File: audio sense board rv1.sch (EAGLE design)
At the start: 32 parts, among them IC1 A000053, IC2 TSOP38238, J1 PJRAN1X1U01X, J4 PJRAN1X1U01X, Q1 2N3904, Q2 2N3904

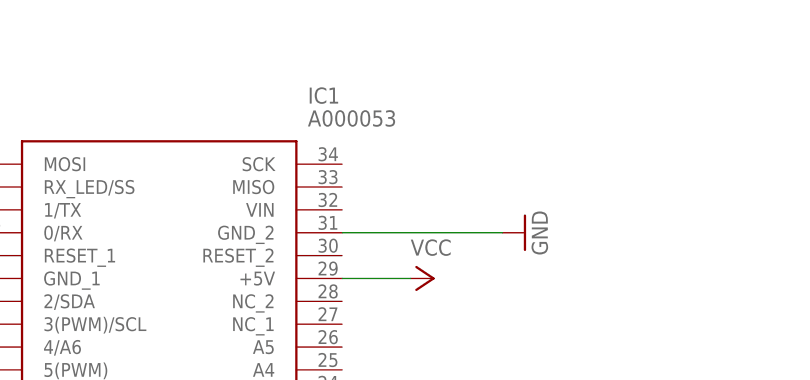
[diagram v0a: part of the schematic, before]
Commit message: add ground pour on bottom
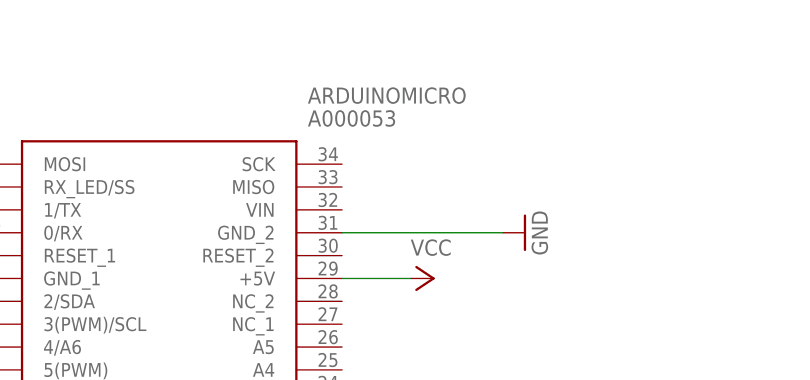
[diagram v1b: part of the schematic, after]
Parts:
- renumbered IC1 to ARDUINOMICRO
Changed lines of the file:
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@@
 <part name="R6" library="Samac Populated" deviceset="CRCW120610K0FKEAC" device="" value="10K"/>
 <part name="GND1" library="supply1" library_urn="urn:adsk.eagle:library:371" deviceset="GND" device=""/>
-<part name="IC1" library="Samac Populated" deviceset="A000053" device=""/>
+<part name="ARDUINOMICRO" library="Samac Populated" deviceset="A000053" device=""/>
 <part name="GND3" library="supply1" library_urn="urn:adsk.eagle:library:371" deviceset="GND" device=""/>
 <part name="LED2" library="SparkFun-LED" library_urn="urn:adsk.eagle:library:529" deviceset="LED" device="1206" package3d_urn="urn:adsk.eagle:package:39352/1" value="LTST-C930GKT"/>
@@
 <attribute name="VALUE" x="30.48" y="15.24" size="1.778" layer="96"/>
 </instance>
-<instance part="IC1" gate="G$1" x="-71.12" y="147.32" smashed="yes">
+<instance part="ARDUINOMICRO" gate="G$1" x="-71.12" y="147.32" smashed="yes">
 <attribute name="NAME" x="-34.29" y="154.94" size="1.778" layer="95" align="center-left"/>
 <attribute name="VALUE" x="-34.29" y="152.4" size="1.778" layer="96" align="center-left"/>
@@
 <wire x1="33.02" y1="55.88" x2="43.18" y2="55.88" width="0.1524" layer="91"/>
 <junction x="33.02" y="55.88"/>
-<pinref part="IC1" gate="G$1" pin="A1"/>
+<pinref part="ARDUINOMICRO" gate="G$1" pin="A1"/>
 <wire x1="43.18" y1="55.88" x2="43.18" y2="116.84" width="0.1524" layer="91"/>
 <wire x1="43.18" y1="116.84" x2="-30.48" y2="116.84" width="0.1524" layer="91"/>
@@
 <segment>
 <pinref part="GND3" gate="1" pin="GND"/>
-<pinref part="IC1" gate="G$1" pin="GND_2"/>
+<pinref part="ARDUINOMICRO" gate="G$1" pin="GND_2"/>
 <wire x1="-12.7" y1="139.7" x2="-30.48" y2="139.7" width="0.1524" layer="91"/>
 </segment>
@@
 <segment>
 <pinref part="GND7" gate="1" pin="GND"/>
-<pinref part="IC1" gate="G$1" pin="GND_1"/>
+<pinref part="ARDUINOMICRO" gate="G$1" pin="GND_1"/>
 </segment>
 </net>
@@
 <segment>
 <pinref part="R13" gate="G$1" pin="2"/>
-<pinref part="IC1" gate="G$1" pin="11(PWM)"/>
+<pinref part="ARDUINOMICRO" gate="G$1" pin="11(PWM)"/>
 <wire x1="-81.28" y1="109.22" x2="-71.12" y2="109.22" width="0.1524" layer="91"/>
 </segment>
@@
 <segment>
 <wire x1="-83.82" y1="157.48" x2="-83.82" y2="132.08" width="0.1524" layer="91"/>
-<pinref part="IC1" gate="G$1" pin="2/SDA"/>
+<pinref part="ARDUINOMICRO" gate="G$1" pin="2/SDA"/>
 <wire x1="-83.82" y1="132.08" x2="-71.12" y2="132.08" width="0.1524" layer="91"/>
 <pinref part="IC2" gate="G$1" pin="OUT"/>
@@
 <net name="N$11" class="0">
 <segment>
-<pinref part="IC1" gate="G$1" pin="10(PWM)/A10"/>
+<pinref part="ARDUINOMICRO" gate="G$1" pin="10(PWM)/A10"/>
 <pinref part="R14" gate="G$1" pin="2"/>
 <wire x1="-71.12" y1="111.76" x2="-78.74" y2="111.76" width="0.1524" layer="91"/>
@@
 <wire x1="162.56" y1="55.88" x2="175.26" y2="55.88" width="0.1524" layer="91"/>
 <junction x="162.56" y="55.88"/>
-<pinref part="IC1" gate="G$1" pin="A2"/>
+<pinref part="ARDUINOMICRO" gate="G$1" pin="A2"/>
 <wire x1="175.26" y1="55.88" x2="175.26" y2="119.38" width="0.1524" layer="91"/>
 <wire x1="175.26" y1="119.38" x2="-30.48" y2="119.38" width="0.1524" layer="91"/>
@@
 </segment>
 <segment>
-<pinref part="IC1" gate="G$1" pin="+5V"/>
+<pinref part="ARDUINOMICRO" gate="G$1" pin="+5V"/>
 <pinref part="P+1" gate="VCC" pin="VCC"/>
 <wire x1="-22.86" y1="134.62" x2="-30.48" y2="134.62" width="0.1524" layer="91"/>
@@
 <wire x1="190.5" y1="81.28" x2="68.58" y2="81.28" width="0.1524" layer="91"/>
 <junction x="68.58" y="81.28"/>
-<pinref part="IC1" gate="G$1" pin="A0"/>
+<pinref part="ARDUINOMICRO" gate="G$1" pin="A0"/>
 <wire x1="-30.48" y1="114.3" x2="60.96" y2="114.3" width="0.1524" layer="91"/>
 <wire x1="60.96" y1="114.3" x2="60.96" y2="73.66" width="0.1524" layer="91"/>

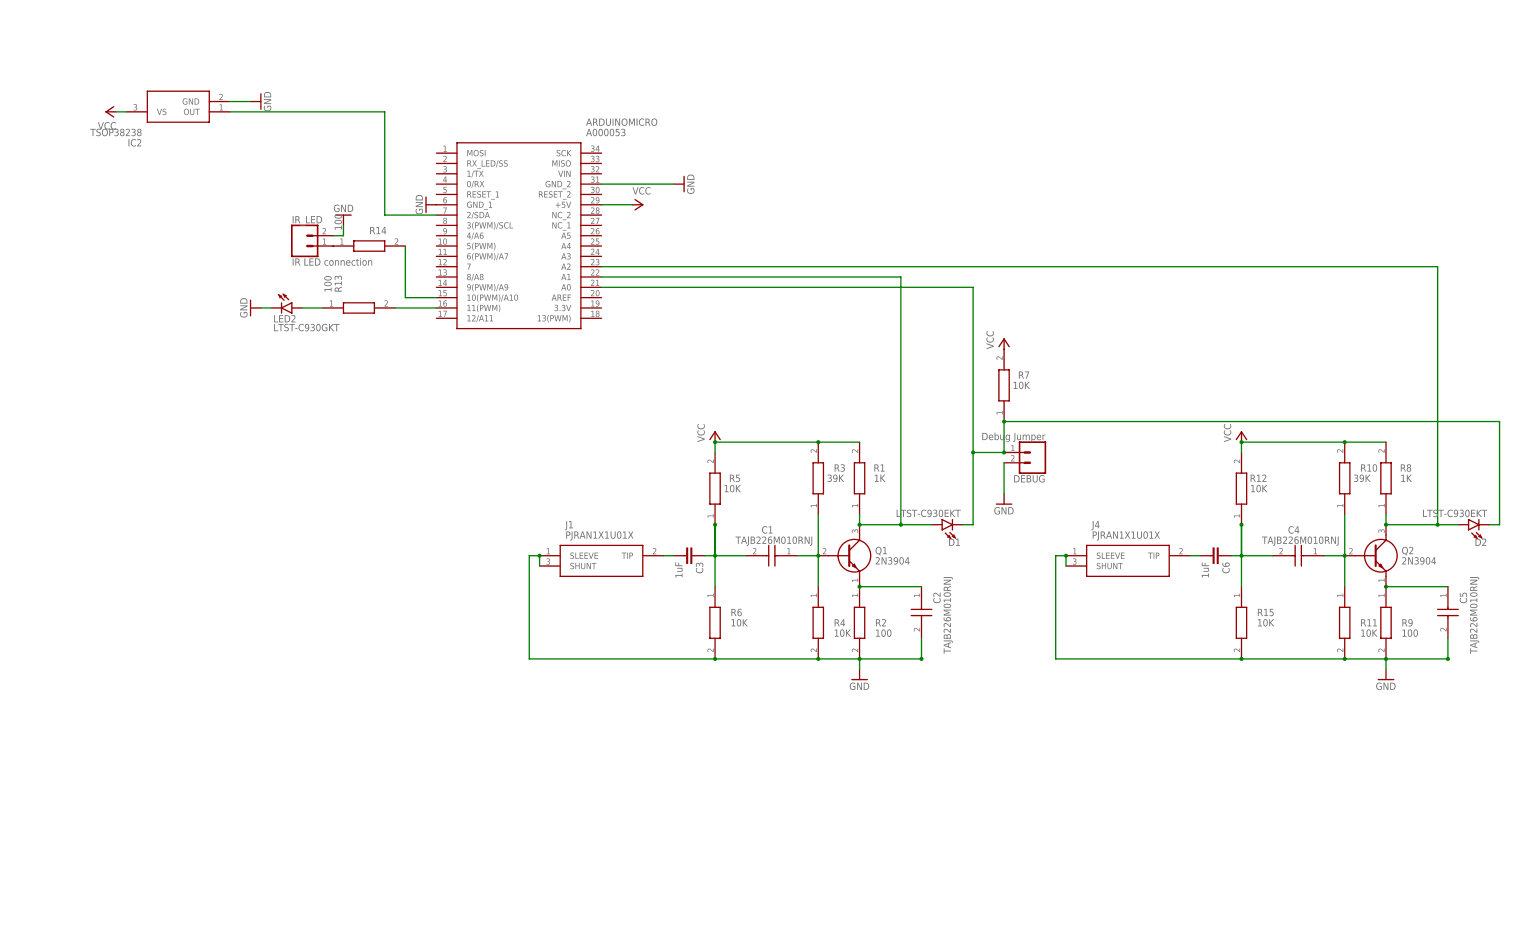
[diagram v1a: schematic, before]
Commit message: rework of circuit, remove LEDs from amp circuit
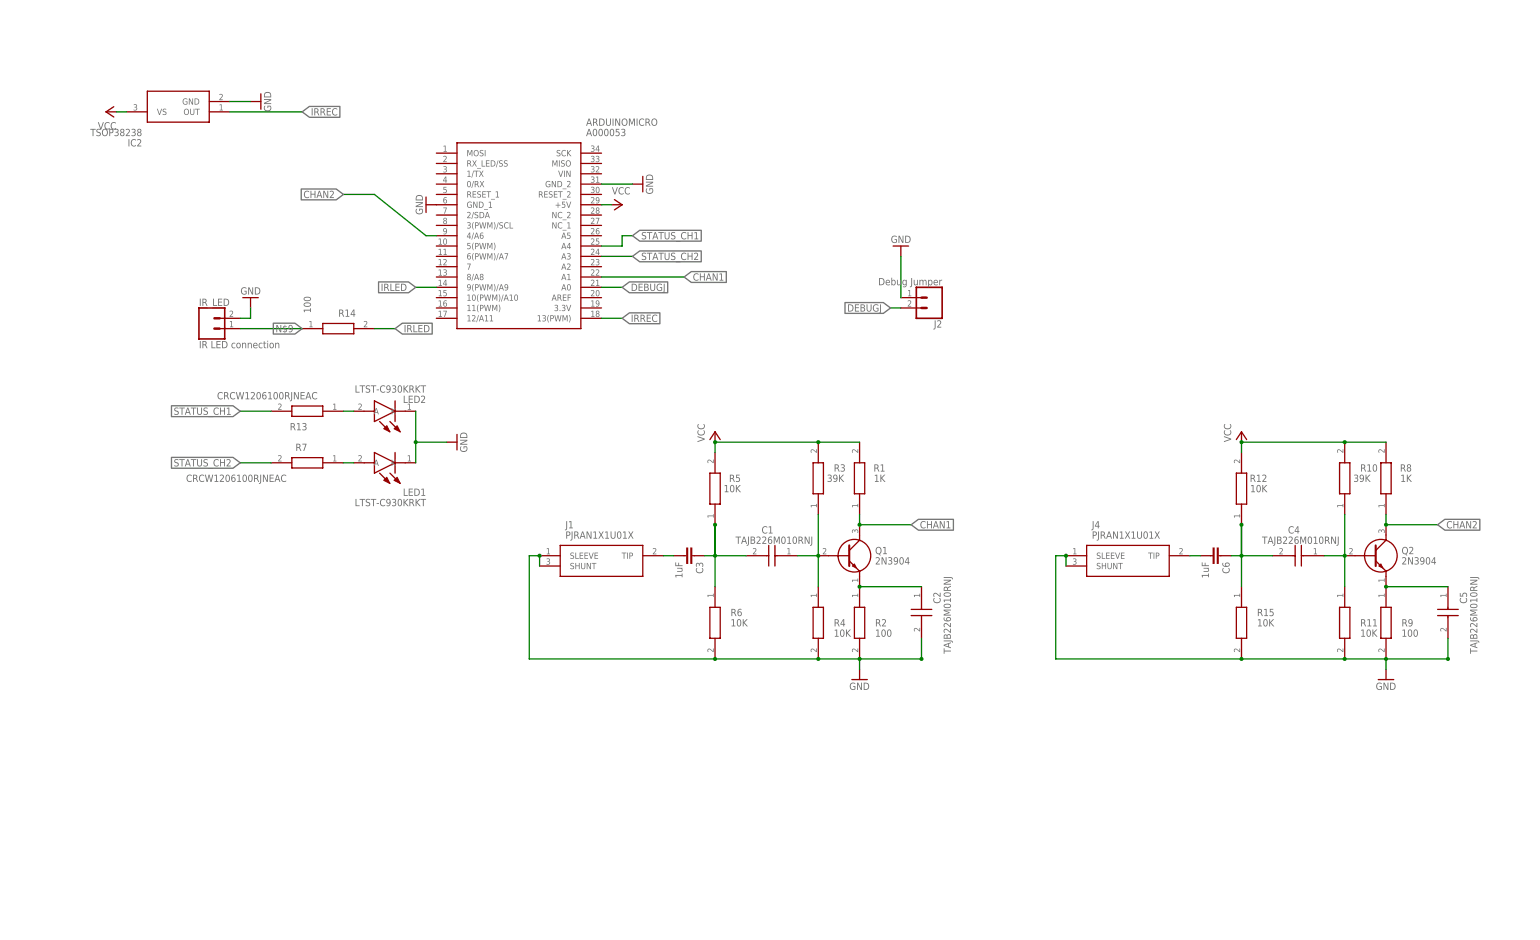
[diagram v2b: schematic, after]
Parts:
- removed D1, D2: LTST-C930EKT, SparkFun-LED:LED1206
- removed DEBUG: Debug Jumper, SparkFun-Connectors:CONN_02LOCK
- added J2: Debug Jumper, SparkFun-Connectors:CONN_02LOCK
- added LED1: LTST-C930KRKT, Samac Populated:LTST-C930KRKT
- LED2: value LTST-C930GKT -> LTST-C930KRKT; device SparkFun-LED:LED1206 -> Samac Populated:LTST-C930KRKT
- R13: value 100 -> CRCW1206100RJNEAC
- R7: value 10K -> CRCW1206100RJNEAC; device Samac Populated:CRCW120610K0FKEAC -> Samac Populated:CRCW1206100RJNEAC
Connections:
- removed net N$11: ARDUINOMICRO.10(PWM)/A10, R14.2
- removed net N$12: ARDUINOMICRO.A2, D2.A, Q2.C, R8.1
- removed net N$15: ARDUINOMICRO.2/SDA, IC2.OUT
- removed net N$2 (its old number): ARDUINOMICRO.A1, D1.A, Q1.C, R1.1
- removed net N$5: ARDUINOMICRO.A0, D1.C, D2.C, DEBUG.1, R7.1
- new net CHAN1: ARDUINOMICRO.A1, Q1.C, R1.1
- new net CHAN2: ARDUINOMICRO.4/A6, Q2.C, R8.1
- new net DEBUGJ: ARDUINOMICRO.A0, J2.2
- new net IRLED: ARDUINOMICRO.9(PWM)/A9, R14.2
- new net IRREC: ARDUINOMICRO.13(PWM), IC2.OUT
- new net STATUS_CH1: ARDUINOMICRO.A4, R13.2
- new net STATUS_CH2: ARDUINOMICRO.A3, R7.2
- net GND: now also J2.1, LED1.K, LED2.K; no longer DEBUG.2, LED2.C
- net N$4: now also LED1.A, R7.1; no longer ARDUINOMICRO.11(PWM), R13.2
- net VCC: no longer R7.2
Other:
- moved on the sheet: IR_LED, R13, R14, R7

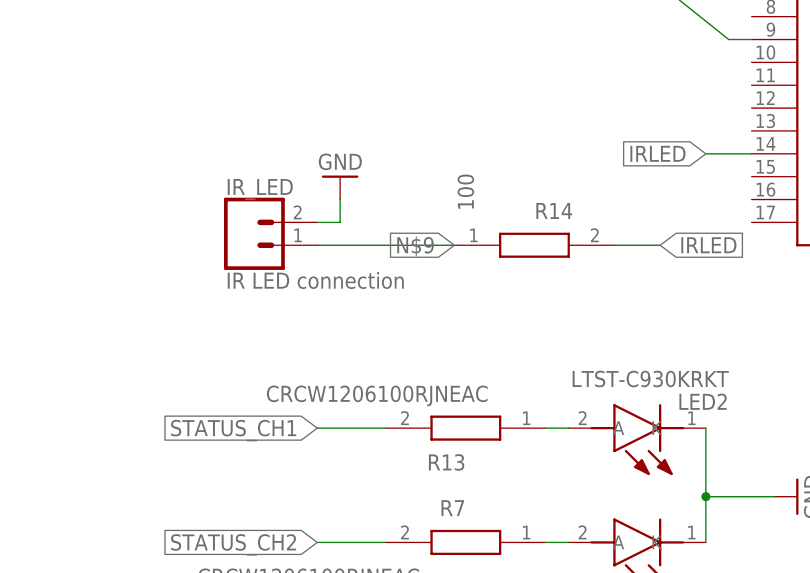
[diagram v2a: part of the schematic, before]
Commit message: update resistors, corners
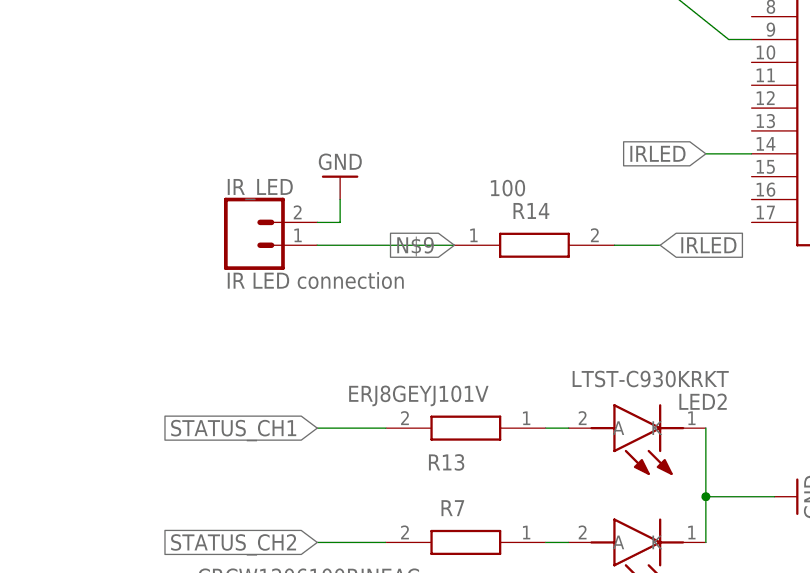
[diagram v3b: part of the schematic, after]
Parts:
- R1: device Samac Populated:CRCW12061K00FKEAC -> Samac Populated:ERJ-8GEYJ102V
- R10, R3: device Samac Populated:CRCW120639K0FKEAC -> Samac Populated:ERJ8GEYJ101V
- R11, R12, R15, R4, R5, R6: device Samac Populated:CRCW120610K0FKEAC -> Samac Populated:ERJ8GEYJ101V
- R13: value CRCW1206100RJNEAC -> ERJ8GEYJ101V; device Samac Populated:CRCW1206100RJNEAC -> Samac Populated:ERJ8GEYJ101V
- R2, R9: device Samac Populated:CRCW1206100RJNEAC -> Samac Populated:ERJ8GEYJ101V
- R8: device Samac Populated:CRCW12061K00FKEAC -> Samac Populated:ERJ8GEYJ101V
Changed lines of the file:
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@@
 <part name="C3" library="SparkFun-Capacitors" library_urn="urn:adsk.eagle:library:510" deviceset="22PF" device="-PTH-2.54MM-200V-5%" package3d_urn="urn:adsk.eagle:package:37435/1" value="1uF"/>
 <part name="Q1" library="Samac Populated" deviceset="2N3904" device=""/>
-<part name="R1" library="Samac Populated" deviceset="CRCW12061K00FKEAC" device="" value="1K"/>
-<part name="R2" library="Samac Populated" deviceset="CRCW1206100RJNEAC" device="" value="100"/>
-<part name="R3" library="Samac Populated" deviceset="CRCW120639K0FKEAC" device="" value="39K"/>
-<part name="R4" library="Samac Populated" deviceset="CRCW120610K0FKEAC" device="" value="10K"/>
-<part name="R5" library="Samac Populated" deviceset="CRCW120610K0FKEAC" device="" value="10K"/>
-<part name="R6" library="Samac Populated" deviceset="CRCW120610K0FKEAC" device="" value="10K"/>
+<part name="R1" library="Samac Populated" deviceset="ERJ-8GEYJ102V" device="" value="1K"/>
+<part name="R2" library="Samac Populated" deviceset="ERJ8GEYJ101V" device="" value="100"/>
+<part name="R3" library="Samac Populated" deviceset="ERJ8GEYJ101V" device="" value="39K"/>
+<part name="R4" library="Samac Populated" deviceset="ERJ8GEYJ101V" device="" value="10K"/>
+<part name="R5" library="Samac Populated" deviceset="ERJ8GEYJ101V" device="" value="10K"/>
+<part name="R6" library="Samac Populated" deviceset="ERJ8GEYJ101V" device="" value="10K"/>
 <part name="GND1" library="supply1" library_urn="urn:adsk.eagle:library:371" deviceset="GND" device=""/>
 <part name="ARDUINOMICRO" library="Samac Populated" deviceset="A000053" device=""/>
@@
 <part name="C6" library="SparkFun-Capacitors" library_urn="urn:adsk.eagle:library:510" deviceset="22PF" device="-PTH-2.54MM-200V-5%" package3d_urn="urn:adsk.eagle:package:37435/1" value="1uF"/>
 <part name="Q2" library="Samac Populated" deviceset="2N3904" device=""/>
-<part name="R8" library="Samac Populated" deviceset="CRCW12061K00FKEAC" device="" value="1K"/>
-<part name="R9" library="Samac Populated" deviceset="CRCW1206100RJNEAC" device="" value="100"/>
-<part name="R10" library="Samac Populated" deviceset="CRCW120639K0FKEAC" device="" value="39K"/>
-<part name="R11" library="Samac Populated" deviceset="CRCW120610K0FKEAC" device="" value="10K"/>
-<part name="R12" library="Samac Populated" deviceset="CRCW120610K0FKEAC" device="" value="10K"/>
-<part name="R15" library="Samac Populated" deviceset="CRCW120610K0FKEAC" device="" value="10K"/>
+<part name="R8" library="Samac Populated" deviceset="ERJ8GEYJ101V" device="" value="1K"/>
+<part name="R9" library="Samac Populated" deviceset="ERJ8GEYJ101V" device="" value="100"/>
+<part name="R10" library="Samac Populated" deviceset="ERJ8GEYJ101V" device="" value="39K"/>
+<part name="R11" library="Samac Populated" deviceset="ERJ8GEYJ101V" device="" value="10K"/>
+<part name="R12" library="Samac Populated" deviceset="ERJ8GEYJ101V" device="" value="10K"/>
+<part name="R15" library="Samac Populated" deviceset="ERJ8GEYJ101V" device="" value="10K"/>
 <part name="GND8" library="supply1" library_urn="urn:adsk.eagle:library:371" deviceset="GND" device=""/>
 <part name="P+1" library="supply1" library_urn="urn:adsk.eagle:library:371" deviceset="VCC" device=""/>
@@
 <part name="LED2" library="Samac Populated" deviceset="LTST-C930KRKT" device=""/>
 <part name="R7" library="Samac Populated" deviceset="CRCW1206100RJNEAC" device=""/>
-<part name="R13" library="Samac Populated" deviceset="CRCW1206100RJNEAC" device=""/>
+<part name="R13" library="Samac Populated" deviceset="ERJ8GEYJ101V" device=""/>
 <part name="GND4" library="supply1" library_urn="urn:adsk.eagle:library:371" deviceset="GND" device=""/>
 <part name="R14" library="Samac Populated" deviceset="CRCW1206100RJNEAC" device="" value="100"/>
@@
 </instance>
 <instance part="R14" gate="G$1" x="-104.14" y="104.14" smashed="yes">
-<attribute name="NAME" x="-95.25" y="107.95" size="1.778" layer="95" align="center-left"/>
-<attribute name="VALUE" x="-102.87" y="107.95" size="1.778" layer="96" rot="R90" align="center-left"/>
+<attribute name="NAME" x="-97.79" y="107.95" size="1.778" layer="95" align="center-left"/>
+<attribute name="VALUE" x="-100.33" y="110.49" size="1.778" layer="96" align="center-left"/>
 </instance>
 </instances>

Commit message: match LED names to channel names
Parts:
- renumbered J2 to DEBUG
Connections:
- net STATUS_CH1: now also R7.2; no longer R13.2
- net STATUS_CH2: now also R13.2; no longer R7.2
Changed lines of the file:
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@@
 <part name="P+5" library="supply1" library_urn="urn:adsk.eagle:library:371" deviceset="VCC" device=""/>
 <part name="GND7" library="supply1" library_urn="urn:adsk.eagle:library:371" deviceset="GND" device=""/>
-<part name="J2" library="SparkFun-Connectors" library_urn="urn:adsk.eagle:library:513" deviceset="CONN_02" device="LOCK" package3d_urn="urn:adsk.eagle:package:38045/1" value="Debug Jumper"/>
+<part name="DEBUG" library="SparkFun-Connectors" library_urn="urn:adsk.eagle:library:513" deviceset="CONN_02" device="LOCK" package3d_urn="urn:adsk.eagle:package:38045/1" value="Debug Jumper"/>
 <part name="GND2" library="supply1" library_urn="urn:adsk.eagle:library:371" deviceset="GND" device=""/>
 <part name="LED1" library="Samac Populated" deviceset="LTST-C930KRKT" device=""/>
@@
 <attribute name="VALUE" x="-76.2" y="137.16" size="1.778" layer="96" rot="R270"/>
 </instance>
-<instance part="J2" gate="G$1" x="50.8" y="111.76" smashed="yes" rot="R180">
+<instance part="DEBUG" gate="G$1" x="50.8" y="111.76" smashed="yes" rot="R180">
 <attribute name="VALUE" x="53.34" y="116.586" size="1.778" layer="96" font="vector" rot="R180"/>
 <attribute name="NAME" x="53.34" y="106.172" size="1.778" layer="95" font="vector" rot="R180"/>
@@
 <segment>
 <pinref part="GND2" gate="1" pin="GND"/>
-<pinref part="J2" gate="G$1" pin="1"/>
+<pinref part="DEBUG" gate="G$1" pin="1"/>
 <wire x1="43.18" y1="121.92" x2="43.18" y2="111.76" width="0.1524" layer="91"/>
 </segment>
@@
 </segment>
 <segment>
-<pinref part="J2" gate="G$1" pin="2"/>
+<pinref part="DEBUG" gate="G$1" pin="2"/>
 <wire x1="43.18" y1="109.22" x2="40.64" y2="109.22" width="0.1524" layer="91"/>
 <label x="40.64" y="109.22" size="1.778" layer="95" rot="R180" xref="yes"/>
@@
 </net>
 <net name="STATUS_CH1" class="0">
-<segment>
-<pinref part="R13" gate="G$1" pin="2"/>
-<wire x1="-111.76" y1="83.82" x2="-119.38" y2="83.82" width="0.1524" layer="91"/>
-<label x="-119.38" y="83.82" size="1.778" layer="95" rot="R180" xref="yes"/>
-</segment>
 <segment>
 <pinref part="ARDUINOMICRO" gate="G$1" pin="A4"/>
@@
 <label x="-22.86" y="127" size="1.778" layer="95" xref="yes"/>
 </segment>
-</net>
-<net name="STATUS_CH2" class="0">
 <segment>
 <pinref part="R7" gate="G$1" pin="2"/>
@@
 <label x="-119.38" y="71.12" size="1.778" layer="95" rot="R180" xref="yes"/>
 </segment>
+</net>
+<net name="STATUS_CH2" class="0">
 <segment>
 <pinref part="ARDUINOMICRO" gate="G$1" pin="A3"/>
@@
 <label x="-22.86" y="121.92" size="1.778" layer="95" xref="yes"/>
 </segment>
-</net>
+<segment>
+<pinref part="R13" gate="G$1" pin="2"/>
+<wire x1="-111.76" y1="83.82" x2="-119.38" y2="83.82" width="0.1524" layer="91"/>
+<label x="-119.38" y="83.82" size="1.778" layer="95" rot="R180" xref="yes"/>
+</segment>
+</net>
